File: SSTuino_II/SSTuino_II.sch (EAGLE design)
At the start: 48 parts, among them J1 TYPE-C-31-M-12, Q1 BSS138PS, Q2 BSS138PW, Q3 BSS138PS, Q4 BSS138PW, U1 MEGA4809, U2 ESP-32S, U3 ATSAMD11D14A-SSNT, U4 74HC4050, U5 74AHC1G125

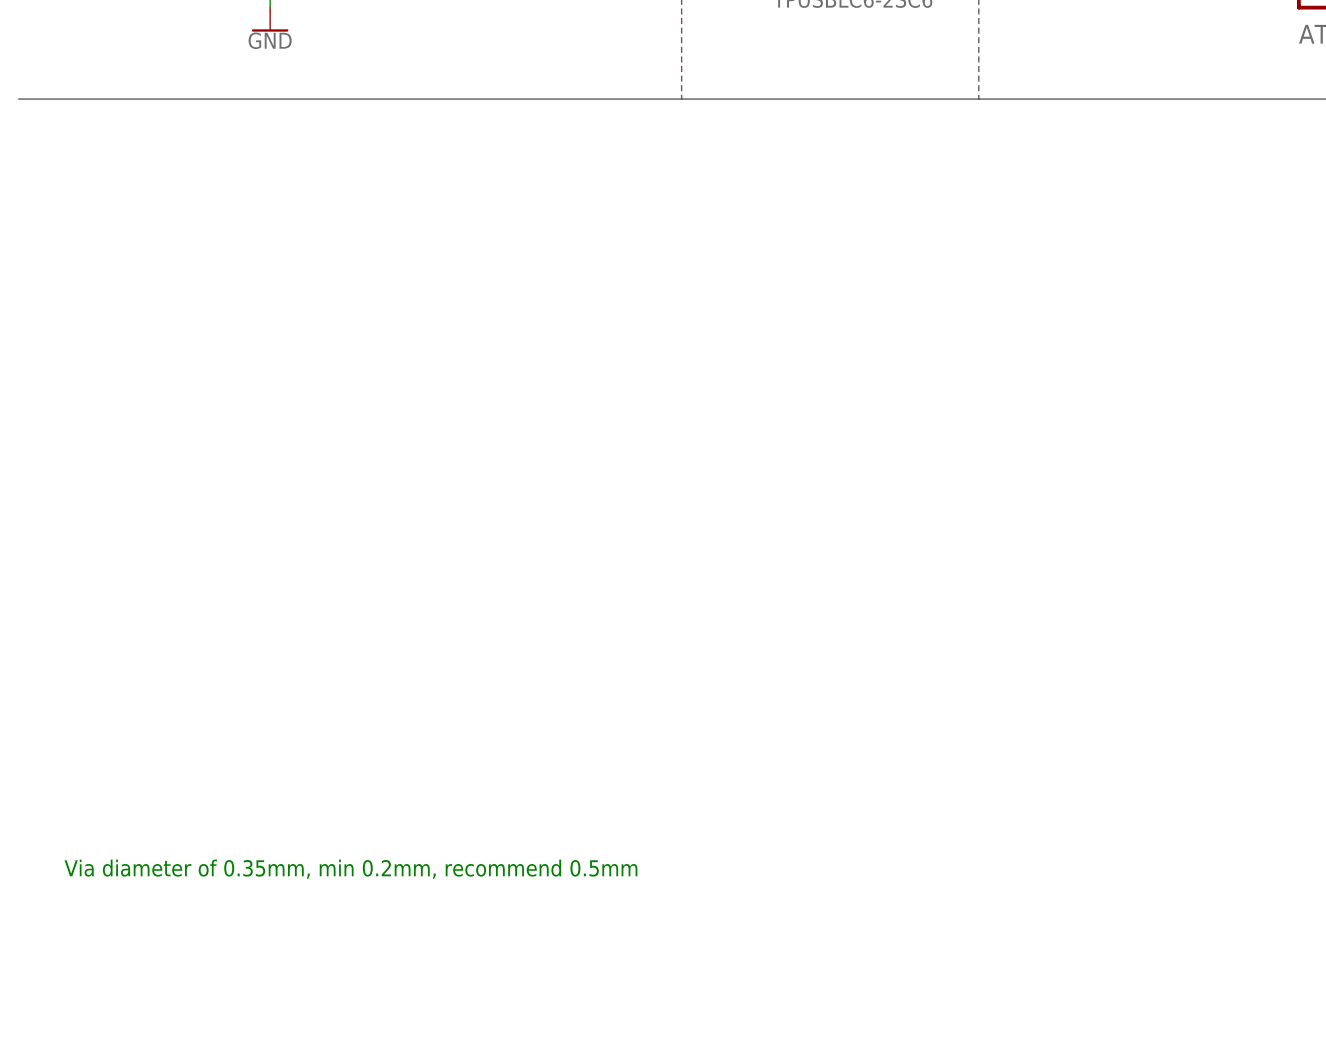
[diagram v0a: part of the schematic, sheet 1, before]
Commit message: added JST SH connector for SPI
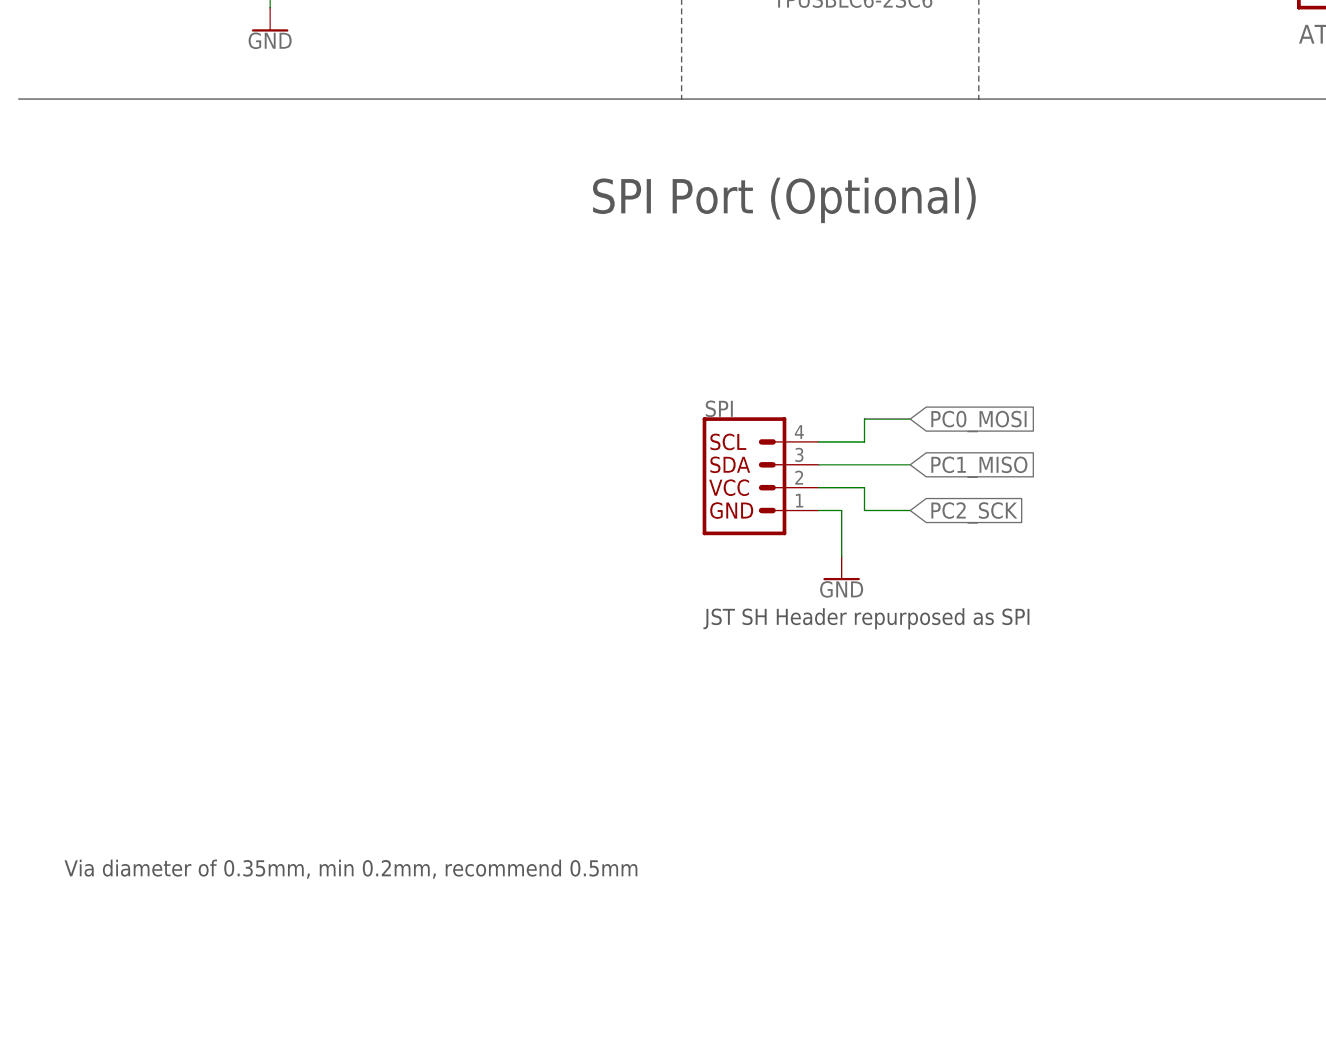
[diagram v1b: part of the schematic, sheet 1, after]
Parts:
- added SPI: (no value), SparkFun-Connectors:QWIIC_CONNECTORJS-1MM
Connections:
- net GND: now also SPI.GND
- net PC0_MOSI: now also SPI.SCL
- net PC1_MISO: now also SPI.SDA
- net PC2_SCK: now also SPI.VCC
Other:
- note added: "JST SH Header repurposed as SPI"
- note added: "SPI Port (Optional)"
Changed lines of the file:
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@@
 <part name="FRAME3" library="SparkFun-Aesthetics" library_urn="urn:adsk.eagle:library:507" deviceset="FRAME-A4L" device=""/>
 <part name="FRAME4" library="SparkFun-Aesthetics" library_urn="urn:adsk.eagle:library:507" deviceset="FRAME-A4L" device=""/>
+<part name="SPI" library="SparkFun-Connectors" library_urn="urn:adsk.eagle:library:513" deviceset="QWIIC_CONNECTOR" device="JS-1MM" package3d_urn="urn:adsk.eagle:package:38096/1"/>
+<part name="GND19" library="SparkFun-PowerSymbols" library_urn="urn:adsk.eagle:library:530" deviceset="GND" device=""/>
 </parts>
 <sheets>
 <sheet>
 <plain>
-<text x="5.08" y="5.08" size="1.778" layer="91">Via diameter of 0.35mm, min 0.2mm, recommend 0.5mm</text>
+<text x="5.08" y="5.08" size="1.778" layer="97">Via diameter of 0.35mm, min 0.2mm, recommend 0.5mm</text>
 <text x="109.22" y="170.18" size="5.08" layer="97">USB Interface</text>
 <wire x1="0" y1="91.44" x2="73.66" y2="91.44" width="0.1524" layer="97"/>
@@
 <text x="218.44" y="-12.7" size="1.9304" layer="97">Pinout Validation:
 Logic Validation: </text>
+<text x="76.2" y="33.02" size="1.778" layer="97">JST SH Header repurposed as SPI</text>
+<text x="63.5" y="78.74" size="3.81" layer="97">SPI Port (Optional)</text>
 </plain>
 <instances>
@@
 <attribute name="NAME" x="236.22" y="109.22" size="1.27" layer="95" font="vector" rot="R90" align="center"/>
 <attribute name="VALUE" x="238.76" y="109.22" size="1.016" layer="96" font="vector" ratio="15" rot="R90" align="center"/>
+</instance>
+<instance part="SPI" gate="J1" x="81.28" y="48.26" smashed="yes">
+<attribute name="VALUE" x="76.2" y="42.926" size="1.778" layer="96" font="vector" align="top-left"/>
+<attribute name="NAME" x="76.2" y="56.134" size="1.778" layer="95" font="vector"/>
+</instance>
+<instance part="GND19" gate="1" x="91.44" y="38.1" smashed="yes">
+<attribute name="VALUE" x="91.44" y="37.846" size="1.778" layer="96" align="top-center"/>
 </instance>
 </instances>
@@
 <junction x="180.34" y="137.16"/>
 </segment>
+<segment>
+<pinref part="SPI" gate="J1" pin="GND"/>
+<wire x1="88.9" y1="45.72" x2="91.44" y2="45.72" width="0.1524" layer="91"/>
+<wire x1="91.44" y1="45.72" x2="91.44" y2="40.64" width="0.1524" layer="91"/>
+<pinref part="GND19" gate="1" pin="GND"/>
+</segment>
 </net>
 <net name="D_P" class="1">
@@
 </segment>
 </net>
+<net name="PC0_MOSI" class="0">
+<segment>
+<pinref part="SPI" gate="J1" pin="SCL"/>
+<wire x1="88.9" y1="53.34" x2="93.98" y2="53.34" width="0.1524" layer="91"/>
+<wire x1="93.98" y1="53.34" x2="93.98" y2="55.88" width="0.1524" layer="91"/>
+<wire x1="93.98" y1="55.88" x2="99.06" y2="55.88" width="0.1524" layer="91"/>
+<label x="99.06" y="55.88" size="1.778" layer="95" xref="yes"/>
+</segment>
+</net>
+<net name="PC1_MISO" class="0">
+<segment>
+<pinref part="SPI" gate="J1" pin="SDA"/>
+<wire x1="88.9" y1="50.8" x2="99.06" y2="50.8" width="0.1524" layer="91"/>
+<label x="99.06" y="50.8" size="1.778" layer="95" xref="yes"/>
+</segment>
+</net>
+<net name="PC2_SCK" class="0">
+<segment>
+<pinref part="SPI" gate="J1" pin="VCC"/>
+<wire x1="88.9" y1="48.26" x2="93.98" y2="48.26" width="0.1524" layer="91"/>
+<wire x1="93.98" y1="48.26" x2="93.98" y2="45.72" width="0.1524" layer="91"/>
+<wire x1="93.98" y1="45.72" x2="99.06" y2="45.72" width="0.1524" layer="91"/>
+<label x="99.06" y="45.72" size="1.778" layer="95" xref="yes"/>
+</segment>
+</net>

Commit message: finalised SSTuino II main board
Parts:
- added J5: (no value), SparkFun-Connectors:CONN_01PTH_NO_SILK_YES_STOP
- J3: device SparkFun-Connectors:CONN_06NO_SILK_FEMALE_PTH -> SparkFun-Connectors:CONN_191X19_NO_SILK
- J4: device SparkFun-Connectors:CONN_191X19_NO_SILK -> SparkFun-Connectors:CONN_06NO_SILK_FEMALE_PTH
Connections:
- net 5V: now also J4.6; no longer J3.6
- net ESP_RX_5V: now also J4.4; no longer J3.4
- net ESP_TX_5V: now also J4.3; no longer J3.3
- net GND: now also J3.15, J4.5; no longer J3.5, J4.15
- net PA0_D2: now also J3.3; no longer J4.3
- net PA1_D7: now also J3.8; no longer J4.8
- net PA2_D20_SDA: now also J3.17; no longer J4.17
- net PA3_D21_SCL: now also J3.18; no longer J4.18
- net PB0_D9~: now also J3.10; no longer J4.10
- net PB1_D10~: now also J3.11; no longer J4.11
- net PB2_D5~: now also J3.6; no longer J4.6
- net PC4_D1_TX1: now also J3.2; no longer J4.2
- net PC5_D0_RX1: now also J3.1; no longer J4.1
- net PC6_D4: now also J3.5; no longer J4.5
- net PD7_A7_AREF: now also J3.16; no longer J4.16
- net PE0_D11: now also J3.12; no longer J4.12
- net PE1_D12: now also J3.13; no longer J4.13
- net PE2_D13: now also J3.14; no longer J4.14
- net PE3_D8: now also J3.9; no longer J4.9
- net PF4_D6~: now also J3.7; no longer J4.7
- net PF5_D3~: now also J3.4; no longer J4.4
- net RESETN: now also J3.19; no longer J4.19
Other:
- note added: "JST SH (Qwiic symbol) Header repurposed as SPI"
- note removed: "JST SH Header repurposed as SPI"
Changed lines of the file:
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@@
 </part>
 <part name="J2" library="SparkFun-Connectors" library_urn="urn:adsk.eagle:library:513" deviceset="CONN_14" device="NO_SILK" package3d_urn="urn:adsk.eagle:package:38187/1"/>
-<part name="J3" library="SparkFun-Connectors" library_urn="urn:adsk.eagle:library:513" deviceset="CONN_06" device="NO_SILK_FEMALE_PTH" package3d_urn="urn:adsk.eagle:package:38130/1"/>
+<part name="J4" library="SparkFun-Connectors" library_urn="urn:adsk.eagle:library:513" deviceset="CONN_06" device="NO_SILK_FEMALE_PTH" package3d_urn="urn:adsk.eagle:package:38130/1"/>
 <part name="SUPPLY11" library="SparkFun-PowerSymbols" library_urn="urn:adsk.eagle:library:530" deviceset="5V" device=""/>
 <part name="GND17" library="SparkFun-PowerSymbols" library_urn="urn:adsk.eagle:library:530" deviceset="GND" device=""/>
@@
 <attribute name="LCSC_PART" value="C784540"/>
 </part>
-<part name="J4" library="SparkFun-Connectors" library_urn="urn:adsk.eagle:library:513" deviceset="CONN_19" device="1X19_NO_SILK" package3d_urn="urn:adsk.eagle:package:38250/1"/>
+<part name="J3" library="SparkFun-Connectors" library_urn="urn:adsk.eagle:library:513" deviceset="CONN_19" device="1X19_NO_SILK" package3d_urn="urn:adsk.eagle:package:38250/1"/>
 <part name="GND18" library="SparkFun-PowerSymbols" library_urn="urn:adsk.eagle:library:530" deviceset="GND" device=""/>
 <part name="RESET" library="D3ltav's Custom" deviceset="SMD-BUTTON(2P-3.9X2.9X1.5+0.4MM)" device="-SKRKAEE020" package3d_urn="urn:adsk.eagle:package:8005100/1" value="TS-1088-AR02016">
@@
 <part name="SPI" library="SparkFun-Connectors" library_urn="urn:adsk.eagle:library:513" deviceset="QWIIC_CONNECTOR" device="JS-1MM" package3d_urn="urn:adsk.eagle:package:38096/1"/>
 <part name="GND19" library="SparkFun-PowerSymbols" library_urn="urn:adsk.eagle:library:530" deviceset="GND" device=""/>
+<part name="J5" library="SparkFun-Connectors" library_urn="urn:adsk.eagle:library:513" deviceset="CONN_01" device="PTH_NO_SILK_YES_STOP" package3d_urn="urn:adsk.eagle:package:38041/1"/>
 </parts>
 <sheets>
@@
 <text x="218.44" y="-12.7" size="1.9304" layer="97">Pinout Validation:
 Logic Validation: </text>
-<text x="76.2" y="33.02" size="1.778" layer="97">JST SH Header repurposed as SPI</text>
+<text x="68.58" y="33.02" size="1.778" layer="97">JST SH (Qwiic symbol) Header repurposed as SPI</text>
 <text x="63.5" y="78.74" size="3.81" layer="97">SPI Port (Optional)</text>
 </plain>
@@
 <text x="30.48" y="7.62" size="1.9304" layer="97">20</text>
 <text x="48.26" y="12.7" size="1.9304" layer="97">19</text>
-<text x="198.12" y="190.5" size="1.9304" layer="97">Pinout Validation:
-Logic Validation: </text>
-<text x="223.52" y="-15.24" size="1.9304" layer="97">Pinout Validation:
-Logic Validation: </text>
-<text x="144.78" y="-15.24" size="1.9304" layer="97">Pinout Validation:
-Logic Validation: </text>
-<text x="48.26" y="-15.24" size="1.9304" layer="97">Pinout Validation:
-Logic Validation: </text>
 </plain>
 <instances>
@@
 <attribute name="NAME" x="31.496" y="63.246" size="1.778" layer="95" font="vector"/>
 </instance>
-<instance part="J3" gate="G$1" x="29.21" y="20.32" smashed="yes" rot="R180">
+<instance part="J4" gate="G$1" x="29.21" y="20.32" smashed="yes" rot="R180">
 <attribute name="VALUE" x="34.29" y="30.226" size="1.778" layer="96" font="vector" rot="R180"/>
 <attribute name="NAME" x="31.242" y="25.4" size="1.778" layer="95" font="vector"/>
@@
 <attribute name="LCSC_PART" x="246.38" y="53.34" size="1.9304" layer="96" display="off"/>
 </instance>
-<instance part="J4" gate="G$1" x="45.72" y="40.64" smashed="yes">
+<instance part="J3" gate="G$1" x="45.72" y="40.64" smashed="yes">
 <attribute name="VALUE" x="45.72" y="12.954" size="1.778" layer="96" font="vector"/>
 <attribute name="NAME" x="46.228" y="63.5" size="1.778" layer="95" font="vector"/>
@@
 <attribute name="LAST_DATE_TIME" x="181.61" y="6.35" size="2.286" layer="94" font="vector"/>
 <attribute name="SHEET" x="195.58" y="1.27" size="2.54" layer="94" font="vector"/>
+</instance>
+<instance part="J5" gate="G$1" x="48.26" y="12.7" smashed="yes">
+<attribute name="VALUE" x="45.72" y="7.874" size="1.778" layer="96" font="vector"/>
+<attribute name="NAME" x="45.72" y="15.748" size="1.778" layer="95" font="vector"/>
 </instance>
 </instances>
@@
 </segment>
 <segment>
-<pinref part="J4" gate="G$1" pin="12"/>
+<pinref part="J3" gate="G$1" pin="12"/>
 <wire x1="55.88" y1="45.72" x2="66.04" y2="45.72" width="0.1524" layer="91"/>
 <label x="55.88" y="45.72" size="1.778" layer="95"/>
@@
 </segment>
 <segment>
-<pinref part="J4" gate="G$1" pin="13"/>
+<pinref part="J3" gate="G$1" pin="13"/>
 <wire x1="55.88" y1="48.26" x2="66.04" y2="48.26" width="0.1524" layer="91"/>
 <label x="55.88" y="48.26" size="1.778" layer="95"/>
@@
 </segment>
 <segment>
-<pinref part="J4" gate="G$1" pin="14"/>
+<pinref part="J3" gate="G$1" pin="14"/>
 <wire x1="55.88" y1="50.8" x2="66.04" y2="50.8" width="0.1524" layer="91"/>
 <label x="55.88" y="50.8" size="1.778" layer="95"/>
@@
 </segment>
 <segment>
-<pinref part="J4" gate="G$1" pin="9"/>
+<pinref part="J3" gate="G$1" pin="9"/>
 <wire x1="55.88" y1="38.1" x2="66.04" y2="38.1" width="0.1524" layer="91"/>
 <label x="55.88" y="38.1" size="1.778" layer="95"/>
@@
 </segment>
 <segment>
-<pinref part="J4" gate="G$1" pin="7"/>
+<pinref part="J3" gate="G$1" pin="7"/>
 <wire x1="55.88" y1="33.02" x2="66.04" y2="33.02" width="0.1524" layer="91"/>
 <label x="55.88" y="33.02" size="1.778" layer="95"/>
@@
 </segment>
 <segment>
-<pinref part="J4" gate="G$1" pin="4"/>
+<pinref part="J3" gate="G$1" pin="4"/>
 <wire x1="55.88" y1="25.4" x2="66.04" y2="25.4" width="0.1524" layer="91"/>
 <label x="55.88" y="25.4" size="1.778" layer="95"/>
@@
 </segment>
 <segment>
-<pinref part="J4" gate="G$1" pin="16"/>
+<pinref part="J3" gate="G$1" pin="16"/>
 <wire x1="55.88" y1="55.88" x2="66.04" y2="55.88" width="0.1524" layer="91"/>
 <label x="55.88" y="55.88" size="1.778" layer="95"/>
@@
 </segment>
 <segment>
-<pinref part="J4" gate="G$1" pin="2"/>
+<pinref part="J3" gate="G$1" pin="2"/>
 <wire x1="55.88" y1="20.32" x2="66.04" y2="20.32" width="0.1524" layer="91"/>
 <label x="55.88" y="20.32" size="1.778" layer="95"/>
@@
 </segment>
 <segment>
-<pinref part="J4" gate="G$1" pin="1"/>
+<pinref part="J3" gate="G$1" pin="1"/>
 <wire x1="55.88" y1="17.78" x2="66.04" y2="17.78" width="0.1524" layer="91"/>
 <label x="55.88" y="17.78" size="1.778" layer="95"/>
@@
 </segment>
 <segment>
-<pinref part="J4" gate="G$1" pin="5"/>
+<pinref part="J3" gate="G$1" pin="5"/>
 <wire x1="55.88" y1="27.94" x2="66.04" y2="27.94" width="0.1524" layer="91"/>
 <label x="55.88" y="27.94" size="1.778" layer="95"/>
@@
 </segment>
 <segment>
-<pinref part="J4" gate="G$1" pin="3"/>
+<pinref part="J3" gate="G$1" pin="3"/>
 <wire x1="55.88" y1="22.86" x2="66.04" y2="22.86" width="0.1524" layer="91"/>
 <label x="55.88" y="22.86" size="1.778" layer="95"/>
@@
 </segment>
 <segment>
-<pinref part="J4" gate="G$1" pin="8"/>
+<pinref part="J3" gate="G$1" pin="8"/>
 <wire x1="55.88" y1="35.56" x2="66.04" y2="35.56" width="0.1524" layer="91"/>
 <label x="55.88" y="35.56" size="1.778" layer="95"/>
@@
 </segment>
 <segment>
-<pinref part="J4" gate="G$1" pin="17"/>
+<pinref part="J3" gate="G$1" pin="17"/>
 <wire x1="55.88" y1="58.42" x2="66.04" y2="58.42" width="0.1524" layer="91"/>
 <label x="55.88" y="58.42" size="1.778" layer="95"/>
@@
 </segment>
 <segment>
-<pinref part="J4" gate="G$1" pin="18"/>
+<pinref part="J3" gate="G$1" pin="18"/>
 <wire x1="55.88" y1="60.96" x2="66.04" y2="60.96" width="0.1524" layer="91"/>
 <label x="55.88" y="60.96" size="1.778" layer="95"/>
@@
 </segment>
 <segment>
-<pinref part="J4" gate="G$1" pin="10"/>
+<pinref part="J3" gate="G$1" pin="10"/>
 <wire x1="55.88" y1="40.64" x2="66.04" y2="40.64" width="0.1524" layer="91"/>
 <label x="55.88" y="40.64" size="1.778" layer="95"/>
@@
 </segment>
 <segment>
-<pinref part="J4" gate="G$1" pin="11"/>
+<pinref part="J3" gate="G$1" pin="11"/>
 <wire x1="55.88" y1="43.18" x2="66.04" y2="43.18" width="0.1524" layer="91"/>
 <label x="55.88" y="43.18" size="1.778" layer="95"/>
@@
 </segment>
 <segment>
-<pinref part="J4" gate="G$1" pin="6"/>
+<pinref part="J3" gate="G$1" pin="6"/>
 <wire x1="55.88" y1="30.48" x2="66.04" y2="30.48" width="0.1524" layer="91"/>
 <label x="55.88" y="30.48" size="1.778" layer="95"/>
@@
 </segment>
 <segment>
-<pinref part="J3" gate="G$1" pin="5"/>
+<pinref part="J4" gate="G$1" pin="5"/>
 <wire x1="24.13" y1="15.24" x2="20.32" y2="15.24" width="0.1524" layer="91"/>
 <pinref part="GND17" gate="1" pin="GND"/>
@@
 </segment>
 <segment>
-<pinref part="J4" gate="G$1" pin="15"/>
+<pinref part="J3" gate="G$1" pin="15"/>
 <wire x1="55.88" y1="53.34" x2="71.12" y2="53.34" width="0.1524" layer="91"/>
 <pinref part="GND18" gate="1" pin="GND"/>
@@
 </segment>
 <segment>
-<pinref part="J3" gate="G$1" pin="6"/>
+<pinref part="J4" gate="G$1" pin="6"/>
 <wire x1="24.13" y1="12.7" x2="7.62" y2="12.7" width="0.1524" layer="91"/>
 <pinref part="SUPPLY11" gate="G$1" pin="5V"/>
@@
 </segment>
 <segment>
-<pinref part="J3" gate="G$1" pin="4"/>
+<pinref part="J4" gate="G$1" pin="4"/>
 <wire x1="24.13" y1="17.78" x2="12.7" y2="17.78" width="0.1524" layer="91"/>
 <label x="10.16" y="17.78" size="1.778" layer="95"/>
@@
 </segment>
 <segment>
-<pinref part="J3" gate="G$1" pin="3"/>
+<pinref part="J4" gate="G$1" pin="3"/>
 <wire x1="24.13" y1="20.32" x2="12.7" y2="20.32" width="0.1524" layer="91"/>
 <label x="10.16" y="20.32" size="1.778" layer="95"/>
@@
 <net name="RESETN" class="0">
 <segment>
-<pinref part="J4" gate="G$1" pin="19"/>
+<pinref part="J3" gate="G$1" pin="19"/>
 <wire x1="55.88" y1="63.5" x2="66.04" y2="63.5" width="0.1524" layer="91"/>
 <label x="55.88" y="63.5" size="1.778" layer="95"/>
